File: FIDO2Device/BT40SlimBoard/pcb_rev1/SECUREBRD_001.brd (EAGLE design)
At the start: 30 x 30 mm, 32 parts, among them CN1 2137160001, CN2 IF_4PIN, CN4 IF_3PIN_SOL, SW3 SKTADAE010, SW4 SKRPACE010, SW5 SKRPACE010, U1 BT40, U3 ADP122ACPZ-3.3-R7

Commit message: 回路図を更新
・プログラミングI/F部に、リセットピンを追加
（PCA10095からファームウェア書込み時、BT40に対してリセット指示できるようにするための措置）
・一部の部品番号を変更
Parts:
- removed C10, C11: 1uF, Parts:C0603K
- removed R6: 1.2k, Parts:R0402
- added C1, C2: 4.7uF, Parts:C0603K
- added R1: 5.1k, Parts:R0402
- C3: value 4.7uF -> 0.01uF; device Parts:C0603K -> Parts:C0402K
- C4: value 4.7uF -> 0.1uF; device Parts:C0603K -> Parts:C0402K
- C5: value 0.01uF -> 0.1uF
- C7, C8: value 0.1uF -> 1uF; device Parts:C0402K -> Parts:C0603K
- CN2: value IF_4PIN -> IF_5PIN_H; device Connectors:HEADER_4PIN -> Connectors:HEADER_5PIN
- R2: value 5.1k -> 1.2k
- moved C3 14.2 mm to (16.3, 4.60)
- moved C5 8.78 mm to (19.7, 12.7), turned to 180 degrees
- moved R2 7.88 mm to (13.4, 5.30)
- moved C8 7.06 mm to (26.7, 11.8), turned to 270 degrees
- moved C4 7.01 mm to (16.2, 7.80), turned to 0 degrees
- moved C7 5.47 mm to (10.8, 6.90)
- moved CN2 0.50 mm to (11.8, 16.1)
- renumbered CN4 to CN3, SW4 to SW1, SW5 to SW2, U3 to U2
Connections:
- net 0V: now also C1.2, C2.2; no longer C10.2, C11.2
- net LED1: now also R2.1; no longer R6.1
- net N$2: now also R1.2; no longer R2.2
- net N$3: now also C7.1; no longer C10.1
- net N$8: now also R2.2; no longer R6.2
- net RESET: now also CN2.5
- net USB_GND: now also R1.1; no longer R2.1
- net VBUS: now also C3.1; no longer C8.1
- net VBUS_NRF: now also C2.1, C8.1; no longer C11.1, C7.1
- net VDD_NRF: now also C1.1; no longer C3.1
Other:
- board text added: "GND"
- board text added: "PCLK"
- board text added: "PIO"
- board text added: "RST"
- board text added: "VTG"

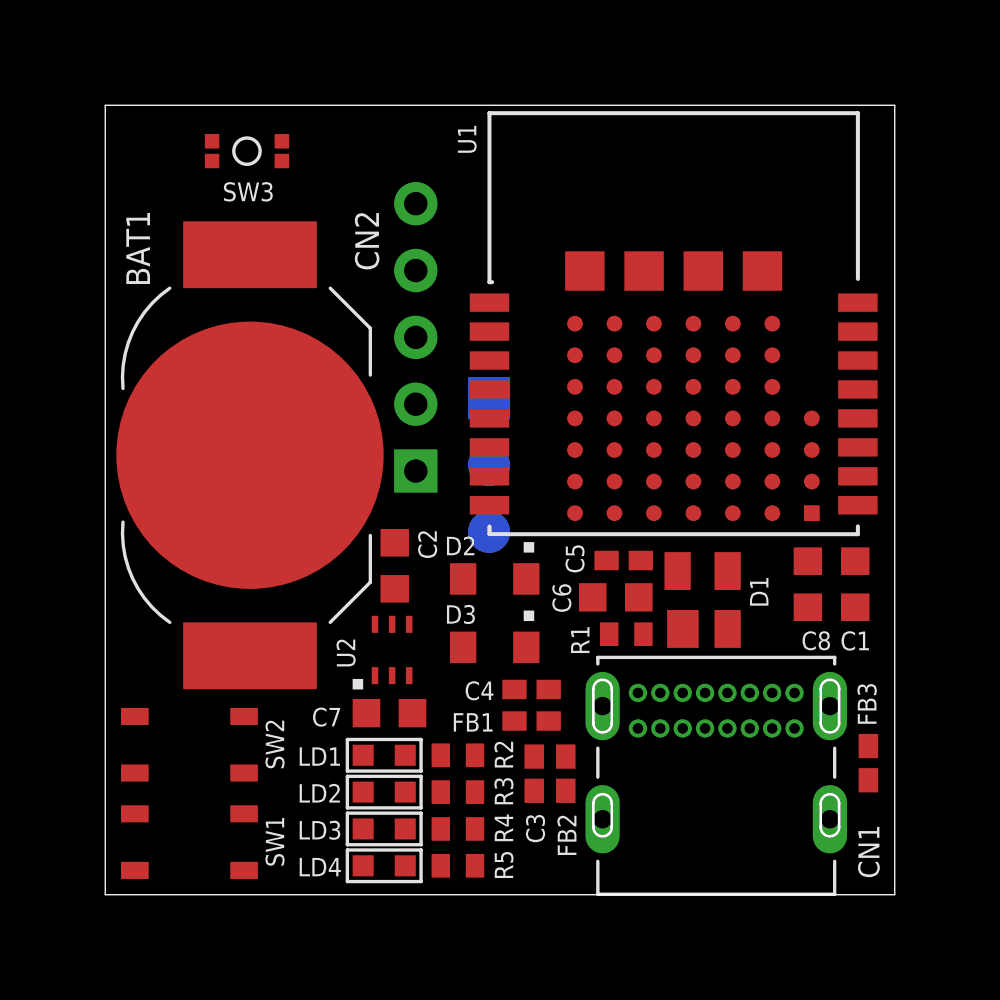
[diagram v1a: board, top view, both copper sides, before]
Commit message: 回路図を更新
・VBUS_NRFのバイパスコンデンサーは不要なので削除
・ユーティリティーI/FにGNDピンを追加
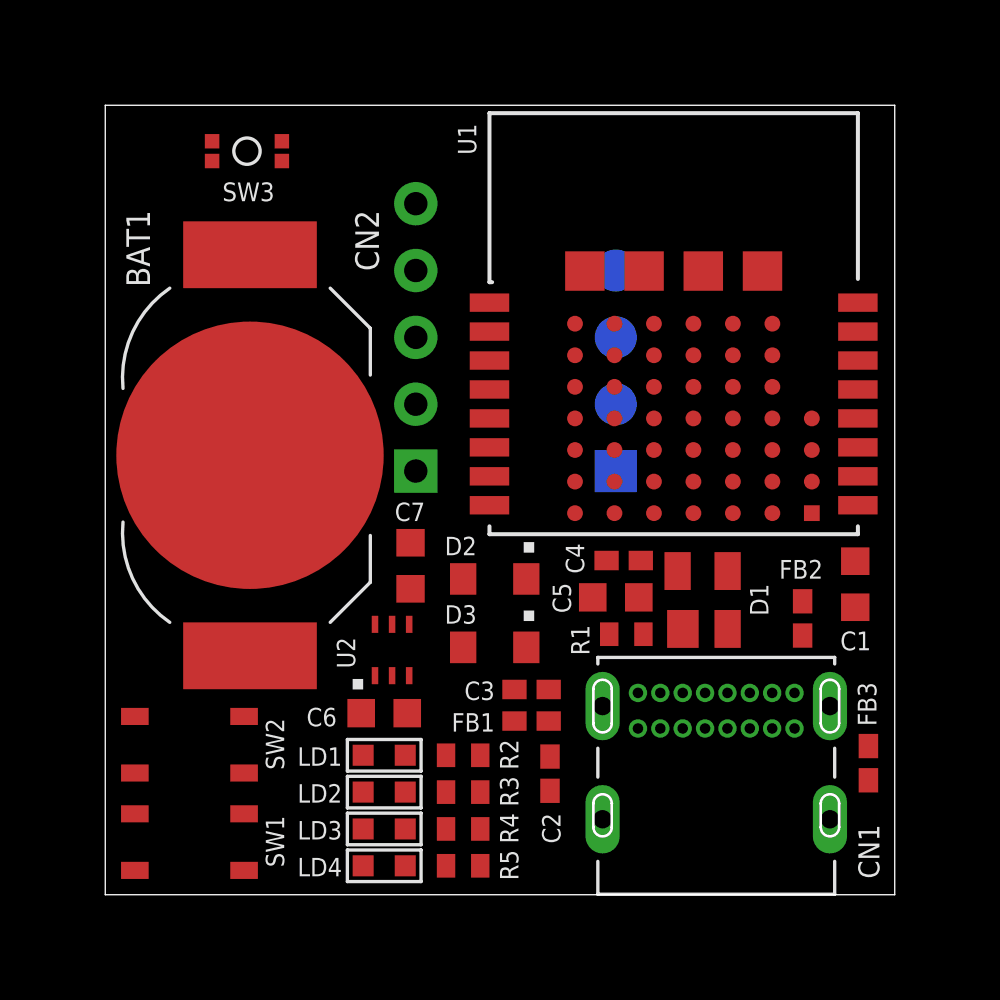
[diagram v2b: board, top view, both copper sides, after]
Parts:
- removed C8: 1uF, Parts:C0603K
- C2: value 4.7uF -> 0.01uF; device Parts:C0603K -> Parts:C0402K
- C3: value 0.01uF -> 0.1uF
- C5: value 0.1uF -> 10uF; device Parts:C0402K -> Parts:C0603K
- C6: value 10uF -> 1uF
- CN3: value IF_3PIN_SOL -> IF_4PIN_SOL; device Connectors:SOLPAD_3PIN -> Connectors:SOLPAD_4PIN
- moved FB2 10.8 mm to (26.5, 10.5), turned to 90 degrees
- moved C2 9.86 mm to (16.9, 4.60), turned to 270 degrees
- moved C6 9.84 mm to (10.6, 6.90), turned to 0 degrees
- moved C4 6.02 mm to (19.7, 12.7), turned to 180 degrees
- moved C7 5.66 mm to (11.6, 12.5), turned to 90 degrees
- moved CN3 5.55 mm to (19.4, 16.1), turned to 90 degrees
- moved C3 3.20 mm to (16.2, 7.80), turned to 0 degrees
- moved C5 1.43 mm to (19.4, 11.3)
- moved R2 0.20 mm to (13.6, 5.30), turned to 180 degrees
- moved R3 0.20 mm to (13.6, 3.90), turned to 180 degrees
- moved R4 0.20 mm to (13.6, 2.50), turned to 180 degrees
- moved R5 0.20 mm to (13.6, 1.10), turned to 180 degrees
- turned FB1 to 180 degrees
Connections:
- net 0V: now also CN3.1; no longer C8.2
- net AIN0: now also CN3.3; no longer CN3.2
- net AIN1: now also CN3.4; no longer CN3.3
- net N$3: now also C6.1; no longer C7.1
- net TXD: now also CN3.2; no longer CN3.1
- net VBUS: now also C2.1, C4.1; no longer C3.1, C6.1
- net VBUS_NRF: now also C3.1, C7.1; no longer C2.1, C4.1, C8.1
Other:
- board text added: "AIN0"
- board text added: "AIN1"
- board text added: "TXD"

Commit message: 配線レイアウトを作成
・べたGND（両面）、差動信号配線まで作成
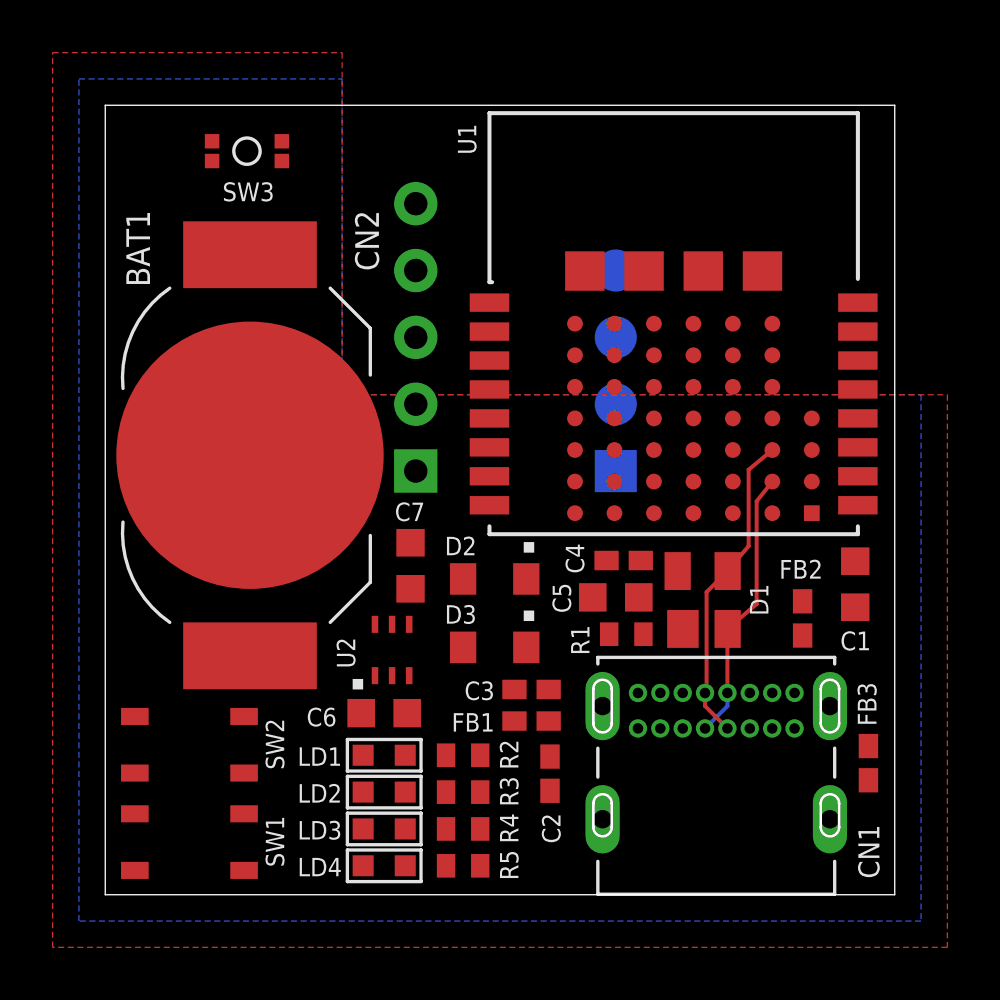
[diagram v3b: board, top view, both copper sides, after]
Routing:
- net D_P: track 0.00 -> 12.0 mm
- net D_N: track 0.00 -> 10.5 mm
- added copper zone on layer 1, net 0V
- added copper zone on layer 16, net 0V
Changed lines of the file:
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@@
 <contactref element="CN2" pad="1"/>
 <contactref element="CN3" pad="1"/>
+<polygon width="0.4064" layer="16" isolate="0.4064" rank="3">
+<vertex x="9" y="31"/>
+<vertex x="9" y="19"/>
+<vertex x="31" y="19"/>
+<vertex x="31" y="-1"/>
+<vertex x="-1" y="-1"/>
+<vertex x="-1" y="31"/>
+</polygon>
+<polygon width="0.4064" layer="1" isolate="0.4064" rank="3">
+<vertex x="-2" y="32"/>
+<vertex x="9" y="32"/>
+<vertex x="9" y="19"/>
+<vertex x="32" y="19"/>
+<vertex x="32" y="-2"/>
+<vertex x="-2" y="-2"/>
+</polygon>
 <wire x1="22.725" y1="23.7" x2="24.975" y2="23.7" width="0" layer="19" extent="1-1"/>
 <wire x1="22.35" y1="21.7" x2="22.725" y2="23.7" width="0" layer="19" extent="1-1"/>
@@
 <wire x1="18.225" y1="23.7" x2="20.475" y2="23.7" width="0" layer="19" extent="1-1"/>
 <wire x1="19.4" y1="16.1" x2="19.35" y2="21.7" width="0" layer="19" extent="1-16"/>
-<wire x1="19.05" y1="12.7" x2="19.4" y2="16.1" width="0" layer="19" extent="1-16"/>
-<wire x1="18.525" y1="11.3" x2="19.05" y2="12.7" width="0" layer="19" extent="1-1"/>
 <wire x1="21.95" y1="10.1" x2="18.525" y2="11.3" width="0" layer="19" extent="1-1"/>
 <wire x1="16.85" y1="7.8" x2="18.525" y2="11.3" width="0" layer="19" extent="1-1"/>
 <wire x1="16.9" y1="3.95" x2="16.85" y2="7.8" width="0" layer="19" extent="1-1"/>
 <wire x1="26.5" y1="11.15" x2="21.95" y2="10.1" width="0" layer="19" extent="1-1"/>
-<wire x1="28.5" y1="10.925" x2="26.5" y2="11.15" width="0" layer="19" extent="1-1"/>
 <wire x1="28.6" y1="15.9" x2="28.5" y2="10.925" width="0" layer="19" extent="1-1"/>
-<wire x1="29" y1="5.65" x2="28.5" y2="10.925" width="0" layer="19" extent="1-1"/>
-<wire x1="11.55" y1="8.325" x2="16.85" y2="7.8" width="0" layer="19" extent="1-1"/>
-<wire x1="11.475" y1="6.9" x2="11.55" y2="8.325" width="0" layer="19" extent="1-1"/>
-<wire x1="11.6" y1="13.375" x2="11.55" y2="8.325" width="0" layer="19" extent="1-1"/>
-<wire x1="11.8" y1="16.1" x2="11.6" y2="13.375" width="0" layer="19" extent="1-1"/>
-<wire x1="5.5" y1="16.7" x2="11.8" y2="16.1" width="0" layer="19" extent="1-1"/>
-<wire x1="5.275" y1="4.625" x2="11.475" y2="6.9" width="0" layer="19" extent="1-1"/>
-<wire x1="5.275" y1="0.925" x2="5.275" y2="4.625" width="0" layer="19" extent="1-1"/>
-<wire x1="1.125" y1="4.625" x2="5.275" y2="4.625" width="0" layer="19" extent="1-1"/>
-<wire x1="1.125" y1="0.925" x2="1.125" y2="4.625" width="0" layer="19" extent="1-1"/>
-<wire x1="4.0596" y1="27.8816" x2="5.5" y2="16.7" width="0" layer="19" extent="1-1"/>
-<wire x1="4.0596" y1="28.6316" x2="4.0596" y2="27.8816" width="0" layer="19" extent="1-1"/>
 </signal>
 <signal name="VBUS_NRF">
@@
 <contactref element="CN1" pad="A7"/>
 <contactref element="CN1" pad="B7"/>
-<wire x1="23.65" y1="10.1" x2="25.35" y2="15.7" width="0" layer="19" extent="1-1"/>
-<wire x1="23.6428" y1="7.6688" x2="23.65" y2="10.1" width="0" layer="19" extent="1-1"/>
-<wire x1="22.7928" y1="6.3188" x2="23.6428" y2="7.6688" width="0" layer="19" extent="1-1"/>
+<wire x1="25.35" y1="15.7" x2="24.7524" y2="14.95" width="0.1524" layer="1"/>
+<wire x1="23.65" y1="10.1" x2="24.7524" y2="11.05" width="0.1524" layer="1"/>
+<wire x1="24.7524" y1="11.05" x2="24.7524" y2="14.95" width="0.1524" layer="1"/>
+<wire x1="23.65" y1="10.1" x2="23.6428" y2="10.0928" width="0.1524" layer="1"/>
+<wire x1="23.6428" y1="10.0928" x2="23.6428" y2="7.6688" width="0.1524" layer="1"/>
+<wire x1="22.7928" y1="6.3188" x2="23.6428" y2="7.1688" width="0.1524" layer="16"/>
+<wire x1="23.6428" y1="7.1688" x2="23.6428" y2="7.6688" width="0.1524" layer="16"/>
 </signal>
 <signal name="D_P">
@@
 <contactref element="CN1" pad="A6"/>
 <contactref element="CN1" pad="B6"/>
-<wire x1="23.65" y1="12.3" x2="25.35" y2="16.9" width="0" layer="19" extent="1-1"/>
-<wire x1="22.7928" y1="7.6688" x2="23.65" y2="12.3" width="0" layer="19" extent="1-1"/>
-<wire x1="23.6428" y1="6.3188" x2="22.7928" y2="7.6688" width="0" layer="19" extent="1-1"/>
+<wire x1="25.35" y1="16.9" x2="24.4476" y2="16.15" width="0.1524" layer="1"/>
+<wire x1="24.4476" y1="16.15" x2="24.4476" y2="13.25" width="0.1524" layer="1"/>
+<wire x1="23.65" y1="12.3" x2="24.4476" y2="13.25" width="0.1524" layer="1"/>
+<wire x1="23.65" y1="12.3" x2="22.85" y2="11.5" width="0.1524" layer="1"/>
+<wire x1="22.85" y1="11.5" x2="22.85" y2="7.726" width="0.1524" layer="1"/>
+<wire x1="22.7928" y1="7.6688" x2="22.85" y2="7.726" width="0.1524" layer="1"/>
+<wire x1="22.7928" y1="7.6688" x2="22.7928" y2="7.1688" width="0.1524" layer="1"/>
+<wire x1="22.7928" y1="7.1688" x2="23.6428" y2="6.3188" width="0.1524" layer="1"/>
 </signal>
 <signal name="LED2">

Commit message: 配線レイアウトを作成
・USBプラグ周りの配線まで作成
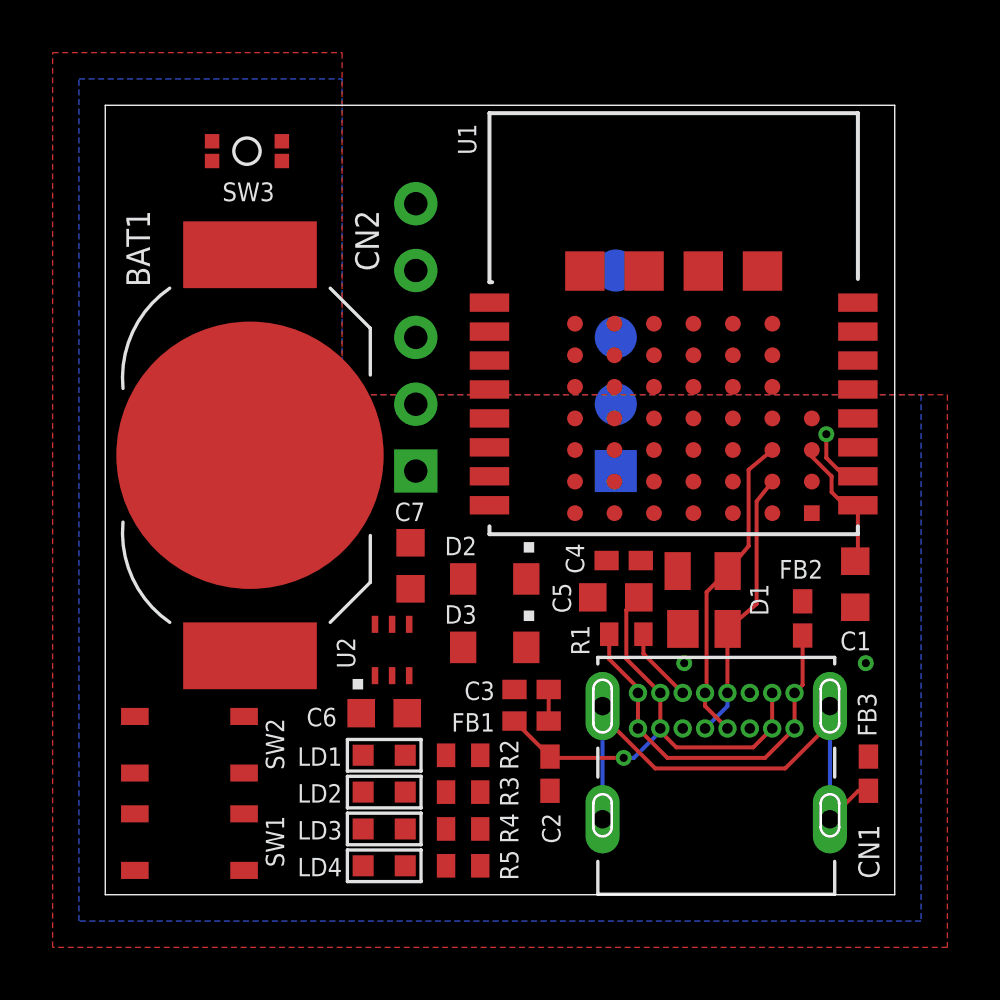
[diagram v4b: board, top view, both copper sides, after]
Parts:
- moved FB3 0.40 mm to (29.0, 4.60)
- turned C3 to 180 degrees
- turned FB1 to 0 degrees
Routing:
- net FG: track 0.00 -> 21.7 mm
- net VBUS: track 0.00 -> 18.6 mm, vias 0 -> 1
- net USB_GND: track 0.00 -> 14.6 mm
- net VDD_NRF: track 0.00 -> 5.28 mm
- net N$2: track 0.00 -> 2.85 mm
- net 0V: track 0.00 -> 2.39 mm, vias 0 -> 3
- net VBUS_NRF: track 0.00 -> 1.20 mm

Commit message: 配線レイアウトを作成
・VBUS〜VDD_NRF周りの配線を作成
・スイッチ、LED周りのviaを作成
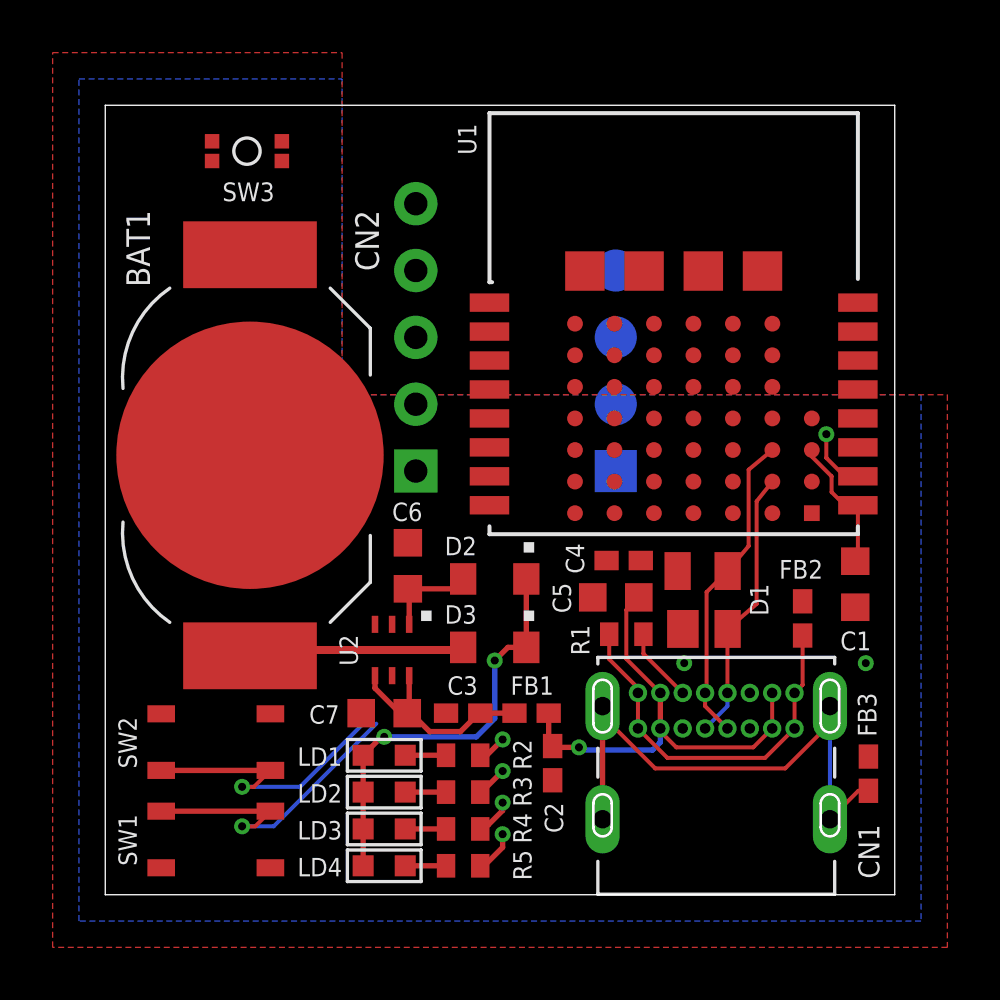
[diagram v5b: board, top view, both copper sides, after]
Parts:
- moved C7 5.69 mm to (10.6, 6.90), turned to 180 degrees
- moved C6 5.67 mm to (11.5, 12.5), turned to 90 degrees
- moved C3 2.75 mm to (13.6, 6.90)
- moved SW1 1.00 mm to (4.20, 2.10)
- moved SW2 1.00 mm to (4.20, 5.80), turned to 180 degrees
- moved C2 0.41 mm to (17.0, 5.00)
- moved FB1 0.30 mm to (16.2, 6.90), turned to 180 degrees
- turned U2 to 180 degrees
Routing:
- net VDD_NRF: track 5.28 -> 21.3 mm, vias 0 -> 2
- net SW1: track 0.00 -> 12.2 mm, vias 0 -> 1
- net SW2: track 0.00 -> 11.4 mm, vias 0 -> 1
- net N$5: track 0.00 -> 8.23 mm
- net VBUS_NRF: track 1.20 -> 8.16 mm
- net N$3: track 0.00 -> 3.63 mm
- net LED4: track 0.00 -> 1.64 mm, vias 0 -> 1
- net N$8: track 0.00 -> 1.55 mm
- net N$7: track 0.00 -> 1.55 mm
- net N$6: track 0.00 -> 1.55 mm
- net N$1: track 0.00 -> 1.55 mm
- net LED3: track 0.00 -> 1.53 mm, vias 0 -> 1
- net LED2: track 0.00 -> 1.18 mm, vias 0 -> 1
- net LED1: track 0.00 -> 1.10 mm, vias 0 -> 1

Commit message: 配線レイアウトを作成
・プログラム信号線、VBUS_NRF、VDD_NRFの配線を作成
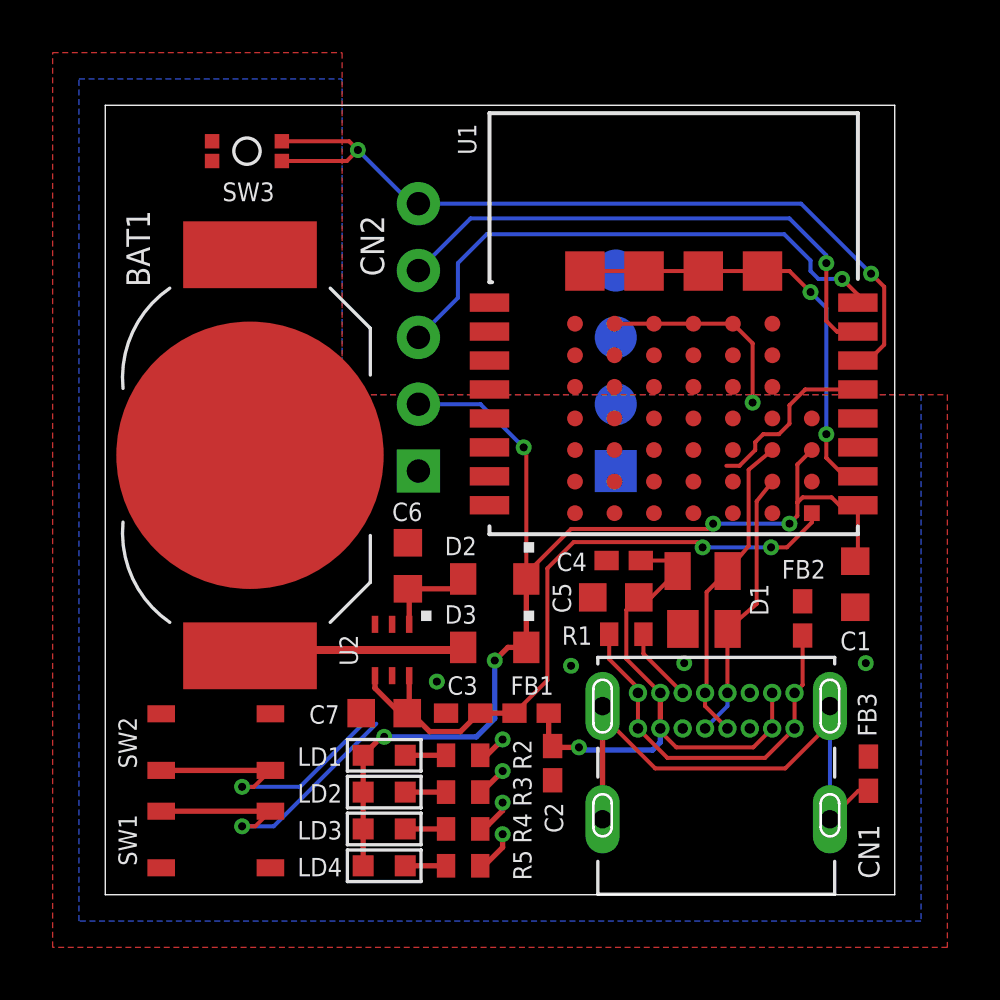
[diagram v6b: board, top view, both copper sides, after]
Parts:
- moved CN2 0.10 mm to (11.9, 16.1)
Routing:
- net RESET: track 0.00 -> 31.7 mm, vias 0 -> 2
- net VDD_NRF: track 21.3 -> 45.0 mm, vias 2 -> 5
- net 0V: track 2.39 -> 24.8 mm, vias 3 -> 7
- net SWCLK: track 0.00 -> 20.8 mm, vias 0 -> 1
- net SWDIO: track 0.00 -> 20.6 mm, vias 0 -> 1
- net VBUS_NRF: track 8.16 -> 25.5 mm, vias 0 -> 2
- net LED3: track 1.53 -> 8.31 mm
- net VBUS: track 18.2 -> 21.7 mm
